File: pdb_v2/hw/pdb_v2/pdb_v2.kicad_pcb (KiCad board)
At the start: 4 copper layers, 92.1 x 66.3 mm, 75 parts, among them J1 XT30-M_Ver, J2 JST-PH_01x02, J3 Conn_01x06_Pin, J5 JST-PH_01x02, J6 Conn_01x03, J7 Conn_01x03, J8 Conn_01x04, Q1 60Vds, U1 LMR51635XFDDCR, U2 ESP32-WROOM-32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

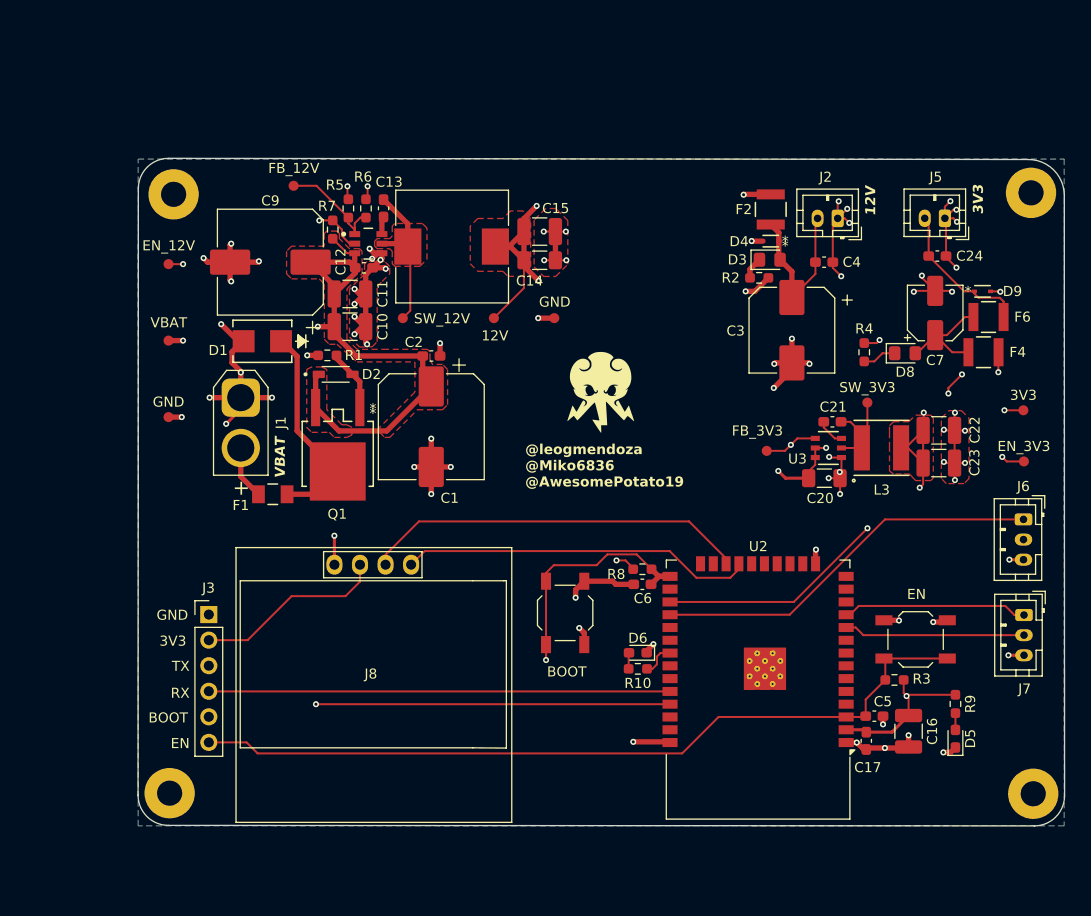
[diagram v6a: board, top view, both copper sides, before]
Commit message: aligned mounting holes
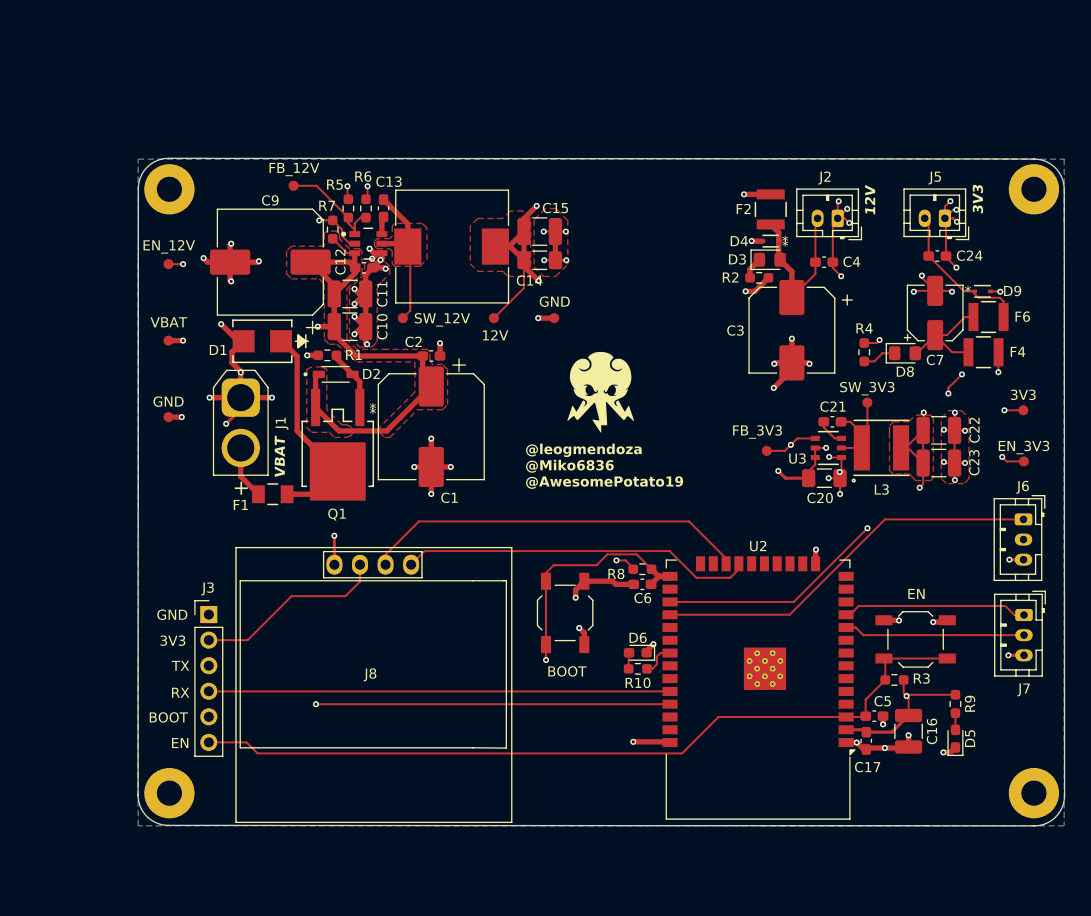
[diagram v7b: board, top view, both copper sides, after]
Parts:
- moved H1 0.65 mm to (15.1, 15.1)
- moved H4 0.45 mm to (101.0, 15.1)
- moved H2 0.09 mm to (101.0, 75.1)
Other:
- outline, holes or cut-outs redrawn
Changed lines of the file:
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@@
 	(footprint "MountingHole:MountingHole_2.5mm_Pad"
 		(layer "F.Cu")
-		(at 100.72 15.45)
+		(at 101.01 15.1)
 		(descr "Mounting Hole 2.5mm, generated by kicad-footprint-generator mountinghole.py")
 		(tags "mountinghole")
@@
 	(footprint "MountingHole:MountingHole_2.5mm_Pad"
 		(layer "F.Cu")
-		(at 15.13 75.1)
+		(at 15.11 75.1)
 		(descr "Mounting Hole 2.5mm, generated by kicad-footprint-generator mountinghole.py")
 		(tags "mountinghole")
@@
 	(footprint "MountingHole:MountingHole_2.5mm_Pad"
 		(layer "F.Cu")
-		(at 15.525 15.6)
+		(at 15.11 15.1)
 		(descr "Mounting Hole 2.5mm, generated by kicad-footprint-generator mountinghole.py")
 		(tags "mountinghole")
@@
 	(footprint "MountingHole:MountingHole_2.5mm_Pad"
 		(layer "F.Cu")
-		(at 100.94 75.16)
+		(at 101.01 75.1)
 		(descr "Mounting Hole 2.5mm, generated by kicad-footprint-generator mountinghole.py")
 		(tags "mountinghole")
@@
 	)
 	(gr_arc
-		(start 100.43 12.140068)
-		(mid 102.958381 13.161403)
-		(end 104.024558 15.671204)
+		(start 101.01 12.09)
+		(mid 103.138002 12.97159)
+		(end 104.019099 15.099795)
 		(stroke
 			(width 0.05)
@@
 	)
 	(gr_line
-		(start 100.43 12.140068)
+		(start 101.01 12.090458)
 		(end 15.02132 12.02132)
 		(stroke
@@
 	)
 	(gr_line
-		(start 104.024558 15.671204)
+		(start 104.019099 15.099795)
 		(end 104.05408 75.3447)
 		(stroke
@@
 	)
 	(segment
-		(start 72.1975 15.6025)
-		(end 72.16 15.64)
-		(width 0.53)
-		(layer "F.Cu")
-		(net 6)
-	)
-	(segment
 		(start 47.0875 20.5875)
 		(end 48.425 20.5875)
@@
 	)
 	(segment
+		(start 72.1975 15.6025)
+		(end 74.86 15.6025)
+		(width 0.53)
+		(layer "F.Cu")
+		(net 6)
+	)
+	(segment
 		(start 50.3375 19.3)
 		(end 50.3375 22.15)
@@
 	)
 	(segment
-		(start 74.86 15.6025)
-		(end 72.1975 15.6025)
-		(width 0.53)
-		(layer "F.Cu")
-		(net 6)
-	)
-	(segment
 		(start 100.01 42.14)
 		(end 98.31 42.14)
@@
 	)
 	(via
-		(at 72.16 15.64)
+		(at 72.1975 15.6025)
 		(size 0.6)
 		(drill 0.3)
@@
 	)
 	(segment
-		(start 72.15 15.65)
-		(end 72.16 15.64)
-		(width 0.53)
-		(layer "In2.Cu")
-		(net 6)
-	)
-	(segment
 		(start 55 27.4)
 		(end 67.2 27.4)
@@
 	)
 	(segment
-		(start 52.7 15.65)
-		(end 72.15 15.65)
-		(width 0.53)
-		(layer "In2.Cu")
-		(net 6)
-	)
-	(segment
 		(start 95.6725 35.6025)
 		(end 95.6725 36.8025)
@@
 	)
 	(segment
+		(start 52.7475 15.6025)
+		(end 51.6 16.75)
+		(width 0.53)
+		(layer "In2.Cu")
+		(net 6)
+	)
+	(segment
 		(start 83.81 34.64)
 		(end 94.71 34.64)
@@
 	)
 	(segment
-		(start 80.66 40.49)
-		(end 80.66 37.79)
-		(width 0.2)
+		(start 72.1975 15.6025)
+		(end 52.7475 15.6025)
+		(width 0.53)
 		(layer "In2.Cu")
 		(net 6)
 	)
 	(segment
-		(start 51.6 16.75)
-		(end 52.7 15.65)
-		(width 0.53)
+		(start 80.66 40.49)
+		(end 80.66 37.79)
+		(width 0.2)
 		(layer "In2.Cu")
 		(net 6)

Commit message: removed diagonal holes
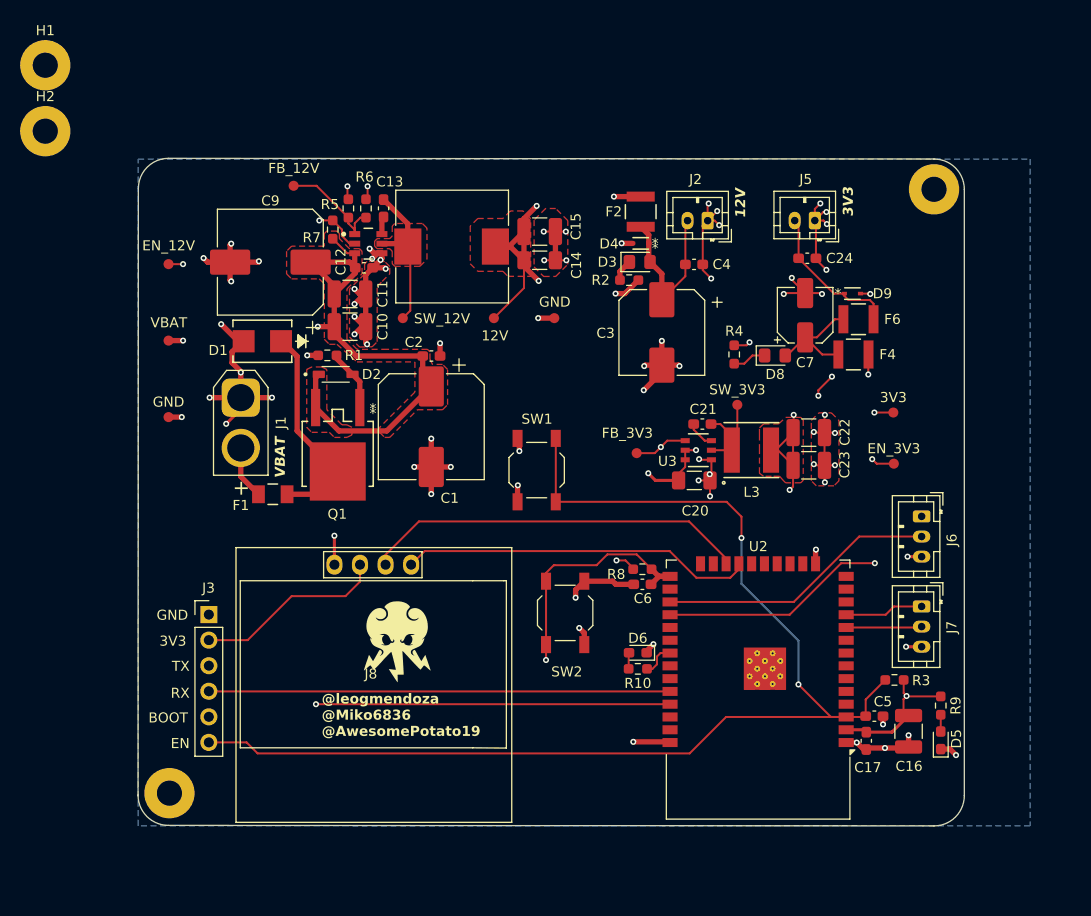
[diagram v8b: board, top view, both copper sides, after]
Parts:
- moved H2 118.2 mm to (2.77, 9.32)
- moved SW1 41.2 mm to (51.6, 43.0), turned to 90 degrees
- moved G*** 32.0 mm to (37.7, 60.0)
- moved H1 17.4 mm to (2.77, 2.77)
- moved U3 12.9 mm to (67.7, 41.0)
- moved D3 12.9 mm to (61.8, 22.3)
- moved 3V3 12.9 mm to (87.0, 37.3)
- moved C20 12.9 mm to (67.3, 44.0)
- moved C21 12.9 mm to (68.1, 38.4)
- moved C22 12.9 mm to (78.6, 39.3)
- moved C23 12.9 mm to (78.6, 42.5)
- moved C24 12.9 mm to (78.5, 22.0)
- moved C3 12.9 mm to (64.0, 29.3)
- moved C4 12.9 mm to (67.2, 22.6)
- moved C7 12.9 mm to (78.3, 27.6)
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- renumbered EN to SW1, BOOT to SW2
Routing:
- net /EN: track 80.1 -> 122.1 mm, vias 0 -> 2
- net /BMS RX: track 38.6 -> 27.7 mm, vias 1 -> 0
- net /VESC TX: track 18.4 -> 7.84 mm
- net /VESC RX: track 18.0 -> 7.54 mm
- net /BMS TX: track 39.0 -> 29.0 mm, vias 0 -> 1
- net 3V3_BUS: track 166.2 -> 165.1 mm
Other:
- board size 92.1 x 66.3 mm -> 82.1 x 66.3 mm
